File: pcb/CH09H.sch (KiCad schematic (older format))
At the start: 4 parts

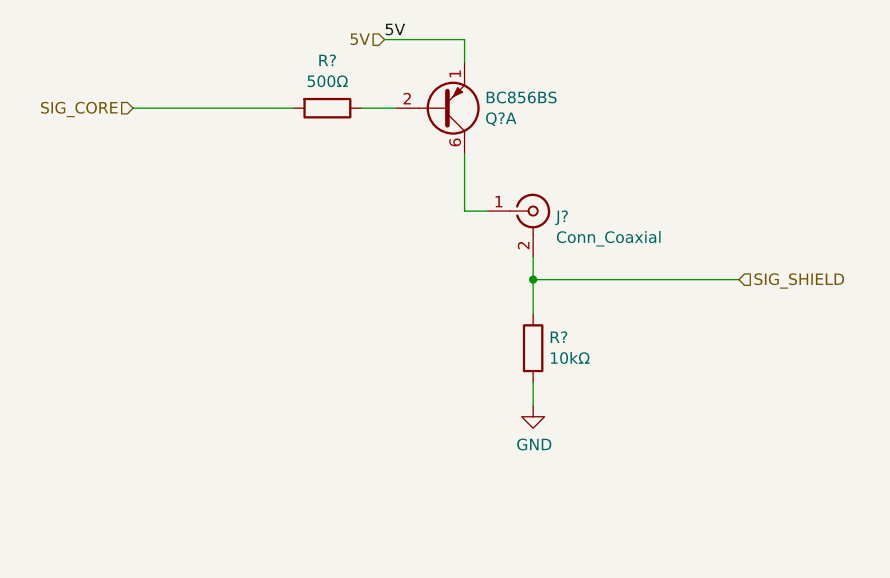
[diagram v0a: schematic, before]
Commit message: Completes first cut of the schematic
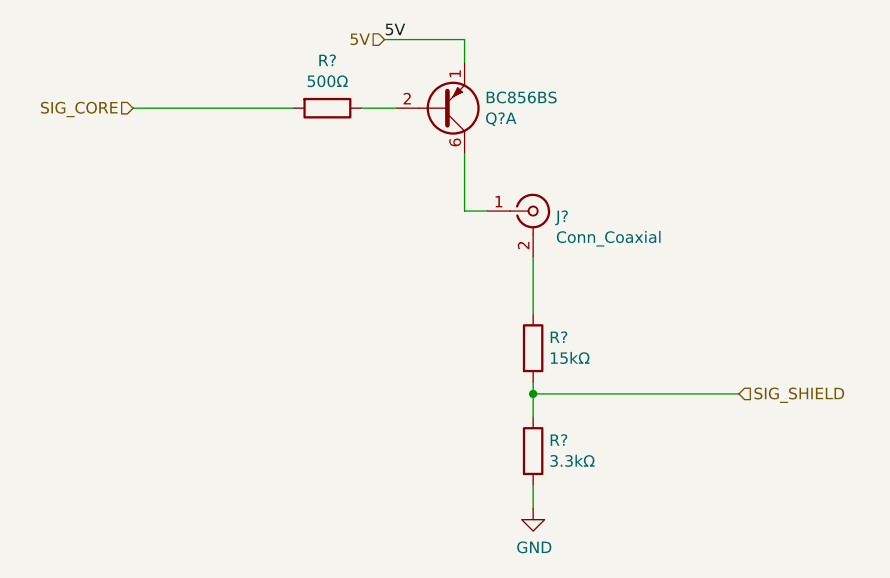
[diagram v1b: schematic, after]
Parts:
- removed R?: 10kΩ, Resistor_SMD:R_0805_2012Metric, symbol Device:R
- added R?: 15kΩ, Resistor_SMD:R_0805_2012Metric, symbol Device:R
- added R?: 3.3kΩ, Resistor_SMD:R_0805_2012Metric, symbol Device:R
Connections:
- net GND: now also R?.2
- net SIG_SHIELD: now also R?.1, R?.2; no longer J?.2 (Ext)
- new net: J?.2 (Ext), R?.1
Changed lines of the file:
@@
 Text Label 3950 1750 0    50   ~ 0
 5V
-$Comp
-L Device:R R?
-U 1 1 61B48182
-P 4600 3100
-AR Path="/61B48182" Ref="R?"  Part="1"
-AR Path="/61B3F4A6/61B48182" Ref="R?"  Part="1"
-AR Path="/61B5B9BC/61B48182" Ref="R?"  Part="1"
-AR Path="/61B7BCED/61B48182" Ref="R?"  Part="1"
-AR Path="/61B8446E/61B48182" Ref="R?"  Part="1"
-AR Path="/61B8A79C/61B48182" Ref="R?"  Part="1"
-AR Path="/61C60B45/61C64A5C/61B48182" Ref="R?"  Part="1"
-F 0 "R?" H 4670 3146 50  0000 L CNN
-F 1 "10kΩ" H 4670 3055 50  0000 L CNN
-F 2 "Resistor_SMD:R_0805_2012Metric" V 4530 3100 50  0001 C CNN
-F 3 "~" H 4600 3100 50  0001 C CNN
-	1    4600 3100
-	1    0    0    -1
-$EndComp
 Wire Wire Line
-	4600 3250 4600 3350
-Wire Wire Line
-	4600 2700 4600 2800
-Wire Wire Line
-	4600 2800 5500 2800
-Connection ~ 4600 2800
-Wire Wire Line
-	4600 2800 4600 2950
+	4600 3300 5500 3300
 $Comp
 L Transistor_BJT:BC856BS Q?
@@
 Wire Wire Line
 	4300 2500 4400 2500
-$Comp
-L power:GND #PWR?
-U 1 1 61B48197
-P 4600 3350
-AR Path="/61B48197" Ref="#PWR?"  Part="1"
-AR Path="/61B3F4A6/61B48197" Ref="#PWR?"  Part="1"
-AR Path="/61B5B9BC/61B48197" Ref="#PWR?"  Part="1"
-AR Path="/61B7BCED/61B48197" Ref="#PWR?"  Part="1"
-AR Path="/61B8446E/61B48197" Ref="#PWR?"  Part="1"
-AR Path="/61B8A79C/61B48197" Ref="#PWR?"  Part="1"
-AR Path="/61C60B45/61C64A5C/61B48197" Ref="#PWR?"  Part="1"
-F 0 "#PWR?" H 4600 3100 50  0001 C CNN
-F 1 "GND" H 4605 3177 50  0000 C CNN
-F 2 "" H 4600 3350 50  0001 C CNN
-F 3 "" H 4600 3350 50  0001 C CNN
-	1    4600 3350
-	1    0    0    -1
-$EndComp
 Text HLabel 2850 2050 0    50   Input ~ 0
 SIG_CORE
 Text HLabel 3950 1750 0    50   Input ~ 0
 5V
-Text HLabel 5500 2800 2    50   Input ~ 0
+Text HLabel 5500 3300 2    50   Input ~ 0
 SIG_SHIELD
+$Comp
+L Device:R R?
+U 1 1 61B774F7
+P 4600 3100
+AR Path="/61B774F7" Ref="R?"  Part="1"
+AR Path="/61B3F4A6/61B774F7" Ref="R?"  Part="1"
+AR Path="/61B5B9BC/61B774F7" Ref="R?"  Part="1"
+AR Path="/61C60B45/61C64A42/61B774F7" Ref="R?"  Part="1"
+AR Path="/61C60B45/61C64A5C/61B774F7" Ref="R?"  Part="1"
+F 0 "R?" H 4670 3146 50  0000 L CNN
+F 1 "15kΩ" H 4670 3055 50  0000 L CNN
+F 2 "Resistor_SMD:R_0805_2012Metric" V 4530 3100 50  0001 C CNN
+F 3 "~" H 4600 3100 50  0001 C CNN
+	1    4600 3100
+	1    0    0    -1
+$EndComp
+Wire Wire Line
+	4600 3700 4600 3800
+$Comp
+L power:GND #PWR?
+U 1 1 61B774FE
+P 4600 3800
+AR Path="/61B774FE" Ref="#PWR?"  Part="1"
+AR Path="/61B3F4A6/61B774FE" Ref="#PWR?"  Part="1"
+AR Path="/61B5B9BC/61B774FE" Ref="#PWR?"  Part="1"
+AR Path="/61C60B45/61C64A42/61B774FE" Ref="#PWR?"  Part="1"
+AR Path="/61C60B45/61C64A5C/61B774FE" Ref="#PWR?"  Part="1"
+F 0 "#PWR?" H 4600 3550 50  0001 C CNN
+F 1 "GND" H 4605 3627 50  0000 C CNN
+F 2 "" H 4600 3800 50  0001 C CNN
+F 3 "" H 4600 3800 50  0001 C CNN
+	1    4600 3800
+	1    0    0    -1
+$EndComp
+$Comp
+L Device:R R?
+U 1 1 61B77504
+P 4600 3550
+AR Path="/61B77504" Ref="R?"  Part="1"
+AR Path="/61B3F4A6/61B77504" Ref="R?"  Part="1"
+AR Path="/61B5B9BC/61B77504" Ref="R?"  Part="1"
+AR Path="/61C60B45/61C64A42/61B77504" Ref="R?"  Part="1"
+AR Path="/61C60B45/61C64A5C/61B77504" Ref="R?"  Part="1"
+F 0 "R?" H 4670 3596 50  0000 L CNN
+F 1 "3.3kΩ" H 4670 3505 50  0000 L CNN
+F 2 "Resistor_SMD:R_0805_2012Metric" V 4530 3550 50  0001 C CNN
+F 3 "~" H 4600 3550 50  0001 C CNN
+	1    4600 3550
+	1    0    0    -1
+$EndComp
+Wire Wire Line
+	4600 3250 4600 3300
+Wire Wire Line
+	4600 2700 4600 2950
+Wire Wire Line
+	4600 3300 4600 3400
+Connection ~ 4600 3300
 $EndSCHEMATC

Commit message: Updates schematic based on some testing. Adds PDF for review
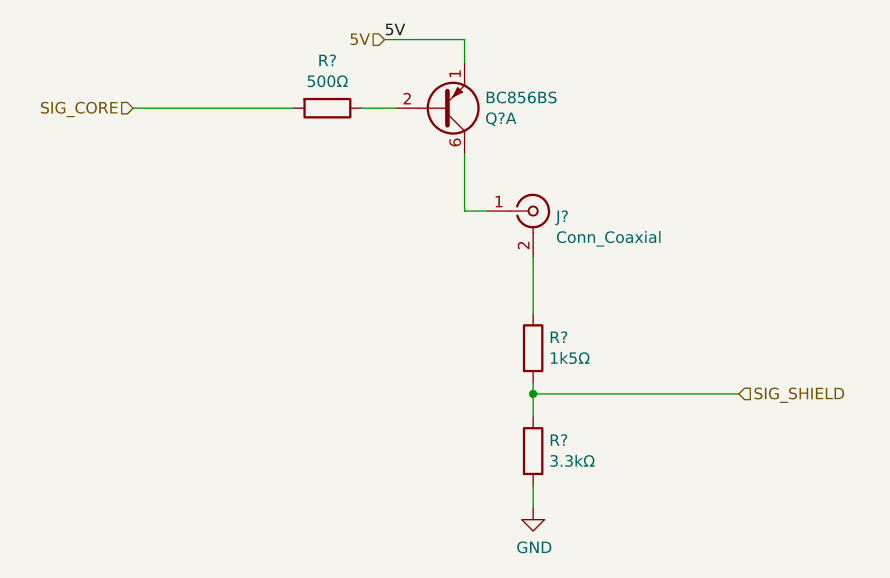
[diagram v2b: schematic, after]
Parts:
- R?: value 15kΩ -> 1k5Ω
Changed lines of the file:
@@
 AR Path="/61C60B45/61C64A5C/61B774F7" Ref="R?"  Part="1"
 F 0 "R?" H 4670 3146 50  0000 L CNN
-F 1 "15kΩ" H 4670 3055 50  0000 L CNN
+F 1 "1k5Ω" H 4670 3055 50  0000 L CNN
 F 2 "Resistor_SMD:R_0805_2012Metric" V 4530 3100 50  0001 C CNN
 F 3 "~" H 4600 3100 50  0001 C CNN
